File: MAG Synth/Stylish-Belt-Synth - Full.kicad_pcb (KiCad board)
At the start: 2 copper layers, 177.8 x 101.7 mm, 61 parts, among them J0 USB_B, J1 Audio-Jack-3_2Switches, J26 WRITE PATCH, J27 PARAM SELECT, J28 PATCH SELECT, J29 MODE, J30 STYLUS, SW1 Power, U1 stm32f103c8t6-module-china, U2 XPT8871

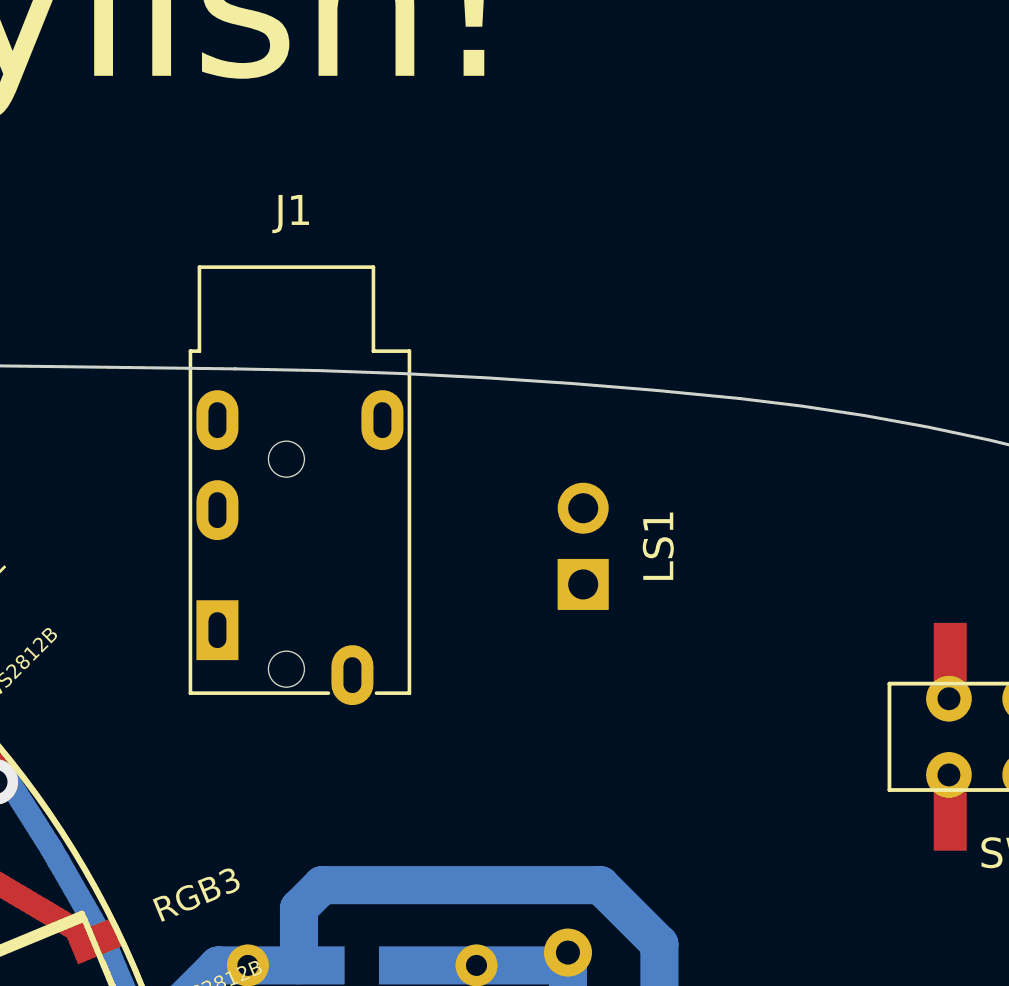
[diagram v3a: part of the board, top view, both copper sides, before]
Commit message: Updated footprints. Including STL for speaker holder.
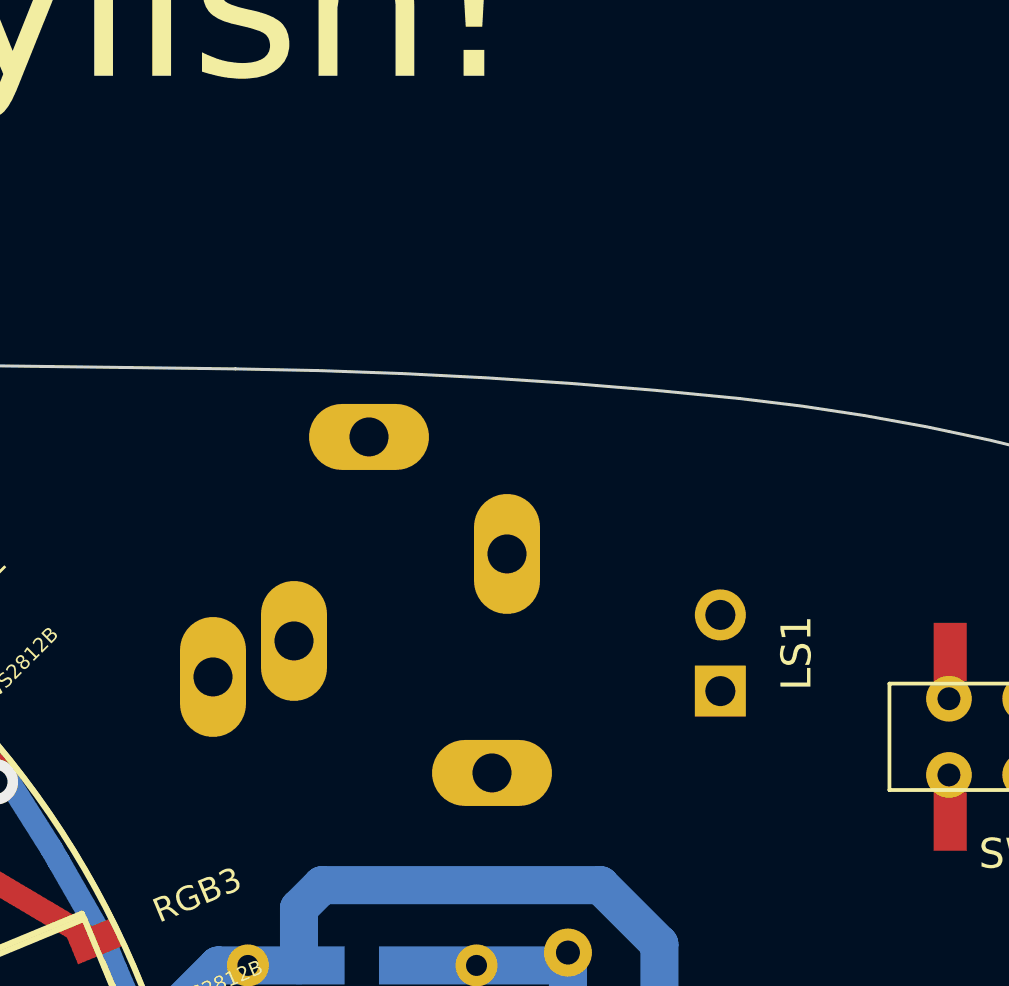
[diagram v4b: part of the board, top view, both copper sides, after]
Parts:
- J1: footprint Connectors:PJ320E_3.5mm_Jack -> Connectors:Stereo_Jack_3.5mm_Switch_Ledino_KB3SPRS; moved to B.Cu
- moved J1 9.98 mm to (188.5, 60.5), turned to 270 degrees
- moved LS1 5.79 mm to (195.6, 65.0)
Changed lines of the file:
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@@
     (add_net "Net-(U1-Pad38)")
   )
+  (module Connectors:Stereo_Jack_3.5mm_Switch_Ledino_KB3SPRS (layer B.Cu)
+    (at 188.468 60.452 270)
+    (descr https://www.reichelt.de/index.html?ACTION=7&LA=3&OPEN=0&INDEX=0&FILENAME=C160%252FKB3SPRS.pdf)
+    (tags "jack stereo TRS")
+    (fp_text reference J1 (at 2.54 13.97 270) (layer B.SilkS)
+      (effects (font (size 1 1) (thickness 0.15)) (justify mirror))
+    )
+    (fp_text value Audio-Jack-3_2Switches (at 2.54 -5.08 270) (layer B.Fab)
+      (effects (font (size 1 1) (thickness 0.15)) (justify mirror))
+    )
+    (fp_line (start -9.3 7.6) (end -9.3 1.6) (layer B.Fab) (width 0.1))
+    (fp_line (start -9.3 1.6) (end -5.7 1.6) (layer B.Fab) (width 0.1))
+    (fp_line (start -9.3 7.6) (end -5.7 7.6) (layer B.Fab) (width 0.1))
+    (fp_line (start -5.7 10.7) (end -5.7 -0.9) (layer B.Fab) (width 0.1))
+    (fp_line (start -5.7 -0.9) (end 8.6 -0.9) (layer B.Fab) (width 0.1))
+    (fp_line (start 8.6 -0.9) (end 8.6 10.7) (layer B.Fab) (width 0.1))
+    (fp_line (start 8.6 10.7) (end -5.7 10.7) (layer B.Fab) (width 0.1))
+    (fp_text user %R (at 2.54 13.97 270) (layer B.Fab)
+      (effects (font (size 1 1) (thickness 0.15)) (justify mirror))
+    )
+    (fp_line (start -9.8 -2) (end 9.1 -2) (layer B.CrtYd) (width 0.05))
+    (fp_line (start 9.1 11.4) (end -9.8 11.4) (layer B.CrtYd) (width 0.05))
+    (fp_line (start -5.8 10.8) (end 2.2 10.8) (layer B.SilkS) (width 0.15))
+    (fp_line (start 6 10.8) (end 8.7 10.8) (layer B.SilkS) (width 0.15))
+    (fp_line (start 8.7 10.8) (end 8.7 -1) (layer B.SilkS) (width 0.15))
+    (fp_line (start 8.7 -1) (end 8.6 -1) (layer B.SilkS) (width 0.15))
+    (fp_line (start 6 -1) (end 1.9 -1) (layer B.SilkS) (width 0.15))
+    (fp_line (start -1.9 -1) (end -5.8 -1) (layer B.SilkS) (width 0.15))
+    (fp_line (start -5.8 -1) (end -5.8 10.8) (layer B.SilkS) (width 0.15))
+    (fp_line (start -5.8 7.7) (end -9.4 7.7) (layer B.SilkS) (width 0.15))
+    (fp_line (start -9.4 7.7) (end -9.4 1.5) (layer B.SilkS) (width 0.15))
+    (fp_line (start -9.4 1.5) (end -5.8 1.5) (layer B.SilkS) (width 0.15))
+    (fp_line (start -9.8 11.4) (end -9.8 -2) (layer B.CrtYd) (width 0.05))
+    (fp_line (start 9.1 -2) (end 9.1 11.4) (layer B.CrtYd) (width 0.05))
+    (pad 1 thru_hole oval (at 0 0 270) (size 4 2.2) (drill 1.3) (layers *.Cu *.Mask)
+      (net 4 /XH-M125-amp-board/OUT+))
+    (pad 4 thru_hole oval (at 7.3 0.5 180) (size 4 2.2) (drill 1.3) (layers *.Cu *.Mask)
+      (net 22 "Net-(J1-Pad4)"))
+    (pad 5 thru_hole oval (at 2.9 7.1 270) (size 4 2.2) (drill 1.3) (layers *.Cu *.Mask)
+      (net 22 "Net-(J1-Pad4)"))
+    (pad 2 thru_hole oval (at 4.1 9.8 270) (size 4 2.2) (drill 1.3) (layers *.Cu *.Mask)
+      (net 4 /XH-M125-amp-board/OUT+))
+    (pad 3 thru_hole oval (at -3.9 4.6 270) (size 2.2 4) (drill 1.3) (layers *.Cu *.Mask)
+      (net 3 /XH-M125-amp-board/OUT-))
+    (model ${KISYS3DMOD}/Connectors.3dshapes/Stereo_Jack_3.5mm_Switch_Ledino_KB3SPRS.wrl
+      (at (xyz 0 0 0))
+      (scale (xyz 1 1 1))
+      (rotate (xyz 0 0 0))
+    )
+  )
   (module SVTmaker:MSS22D18+THT (layer F.Cu)
     (at 205.74 66.548 180)
@@
   )
   (module Pin_Headers:Pin_Header_Straight_1x02_Pitch2.54mm (layer B.Cu)
-    (at 191.008 61.468)
+    (at 195.58 65.024)
     (descr "Through hole straight pin header, 1x02, 2.54mm pitch, single row")
     (tags "Through hole pin header THT 1x02 2.54mm single row")
@@
     )
   )
-  (module Connectors:PJ320E_3.5mm_Jack (layer F.Cu)
-    (at 178.816 62.992)
-    (descr "Headphones with microphone connector, 3.5mm, 4 pins.")
-    (tags "3.5mm jack mic microphone phones headphones 4pins audio plug")
-    (fp_text reference J1 (at 2.54 -13.97) (layer F.SilkS)
-      (effects (font (size 1 1) (thickness 0.15)))
-    )
-    (fp_text value Audio-Jack-3_2Switches (at 2.54 5.08) (layer F.Fab)
-      (effects (font (size 1 1) (thickness 0.15)))
-    )
-    (fp_line (start -1.3 -12.5) (end 6.8 -12.5) (layer F.CrtYd) (width 0.05))
-    (fp_line (start -0.6 -9.3) (end -0.6 -12.1) (layer F.SilkS) (width 0.12))
-    (fp_line (start 5.2 -9.3) (end 5.2 -12.1) (layer F.SilkS) (width 0.12))
-    (fp_line (start 6.4 -9.3) (end 6.4 2.1) (layer F.SilkS) (width 0.12))
-    (fp_line (start 5.2 -12.1) (end -0.6 -12.1) (layer F.SilkS) (width 0.12))
-    (fp_line (start -0.9 -9.3) (end -0.6 -9.3) (layer F.SilkS) (width 0.12))
-    (fp_line (start 5.2 -9.3) (end 6.4 -9.3) (layer F.SilkS) (width 0.12))
-    (fp_line (start 6.8 -12.5) (end 6.8 3) (layer F.CrtYd) (width 0.05))
-    (fp_line (start -1.3 -12.5) (end -1.3 3) (layer F.CrtYd) (width 0.05))
-    (fp_line (start -1.3 3) (end 6.8 3) (layer F.CrtYd) (width 0.05))
-    (fp_line (start 6.4 2.1) (end 5.3 2.1) (layer F.SilkS) (width 0.12))
-    (fp_line (start -0.9 2.1) (end 3.7 2.1) (layer F.SilkS) (width 0.12))
-    (fp_line (start -0.9 -9.3) (end -0.9 2.1) (layer F.SilkS) (width 0.12))
-    (fp_line (start 6.3 2) (end 5.3 2) (layer F.Fab) (width 0.1))
-    (fp_line (start 6.3 -9.2) (end 6.3 2) (layer F.Fab) (width 0.1))
-    (fp_line (start 5.1 -9.2) (end 6.3 -9.2) (layer F.Fab) (width 0.1))
-    (fp_line (start 5.1 -12) (end 5.1 -9.2) (layer F.Fab) (width 0.1))
-    (fp_line (start -0.5 -12) (end 5.1 -12) (layer F.Fab) (width 0.1))
-    (fp_line (start -0.5 -9.2) (end -0.5 -12) (layer F.Fab) (width 0.1))
-    (fp_line (start -0.8 -9.2) (end -0.5 -9.2) (layer F.Fab) (width 0.1))
-    (fp_line (start -0.8 2) (end -0.8 -9.2) (layer F.Fab) (width 0.1))
-    (fp_line (start 3.7 2) (end -0.8 2) (layer F.Fab) (width 0.1))
-    (fp_text user %R (at 2.54 -13.97) (layer F.Fab)
-      (effects (font (size 1 1) (thickness 0.15)))
-    )
-    (pad "" np_thru_hole circle (at 2.3 1.3 270) (size 1.2 1.2) (drill 1.2) (layers *.Cu *.Mask))
-    (pad "" np_thru_hole circle (at 2.3 -5.7 270) (size 1.2 1.2) (drill 1.2) (layers *.Cu *.Mask))
-    (pad 3 thru_hole oval (at 0 -7 270) (size 2 1.4) (drill oval 1.2 0.6) (layers *.Cu *.Mask)
-      (net 3 /XH-M125-amp-board/OUT-))
-    (pad 2 thru_hole oval (at 0 -4 270) (size 2 1.4) (drill oval 1.2 0.6) (layers *.Cu *.Mask)
-      (net 4 /XH-M125-amp-board/OUT+))
-    (pad 1 thru_hole rect (at 0 0 270) (size 2 1.4) (drill oval 1.2 0.6) (layers *.Cu *.Mask)
-      (net 4 /XH-M125-amp-board/OUT+))
-    (pad 4 thru_hole oval (at 4.5 1.5 270) (size 2 1.4) (drill oval 1.2 0.6) (layers *.Cu *.Mask)
-      (net 22 "Net-(J1-Pad4)"))
-    (pad 5 thru_hole oval (at 5.5 -7 270) (size 2 1.4) (drill oval 1.2 0.6) (layers *.Cu *.Mask)
-      (net 22 "Net-(J1-Pad4)"))
-  )
   (gr_text Stylish! (at 189.6364 67.1957) (layer F.Mask)

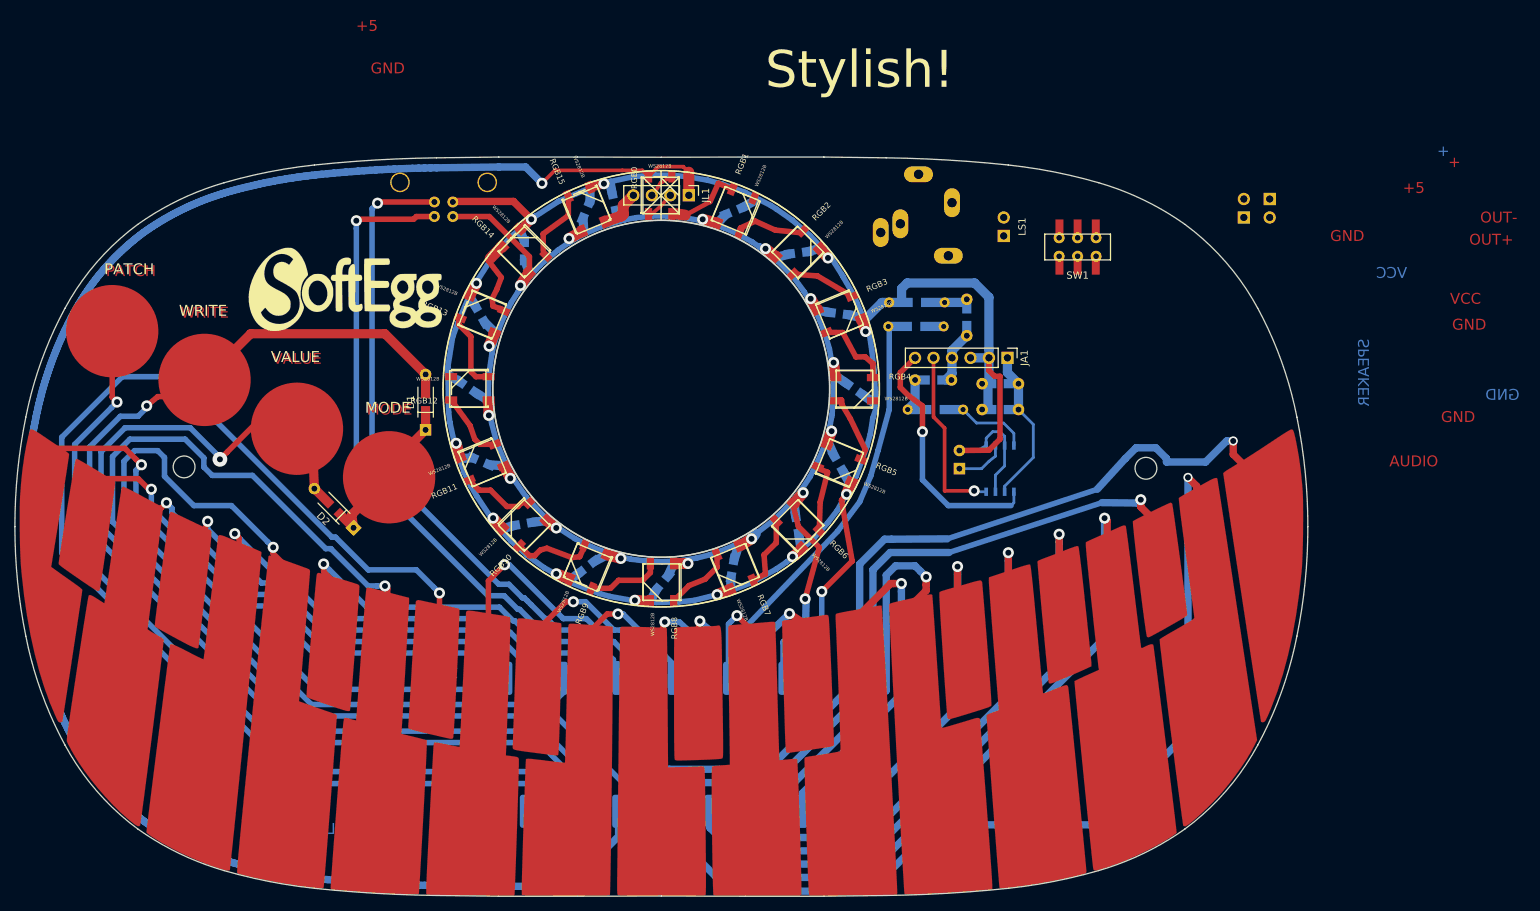
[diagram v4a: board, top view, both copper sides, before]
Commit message: V0.2 PCB completed! Schematic, PCB, and Gerbers updated.
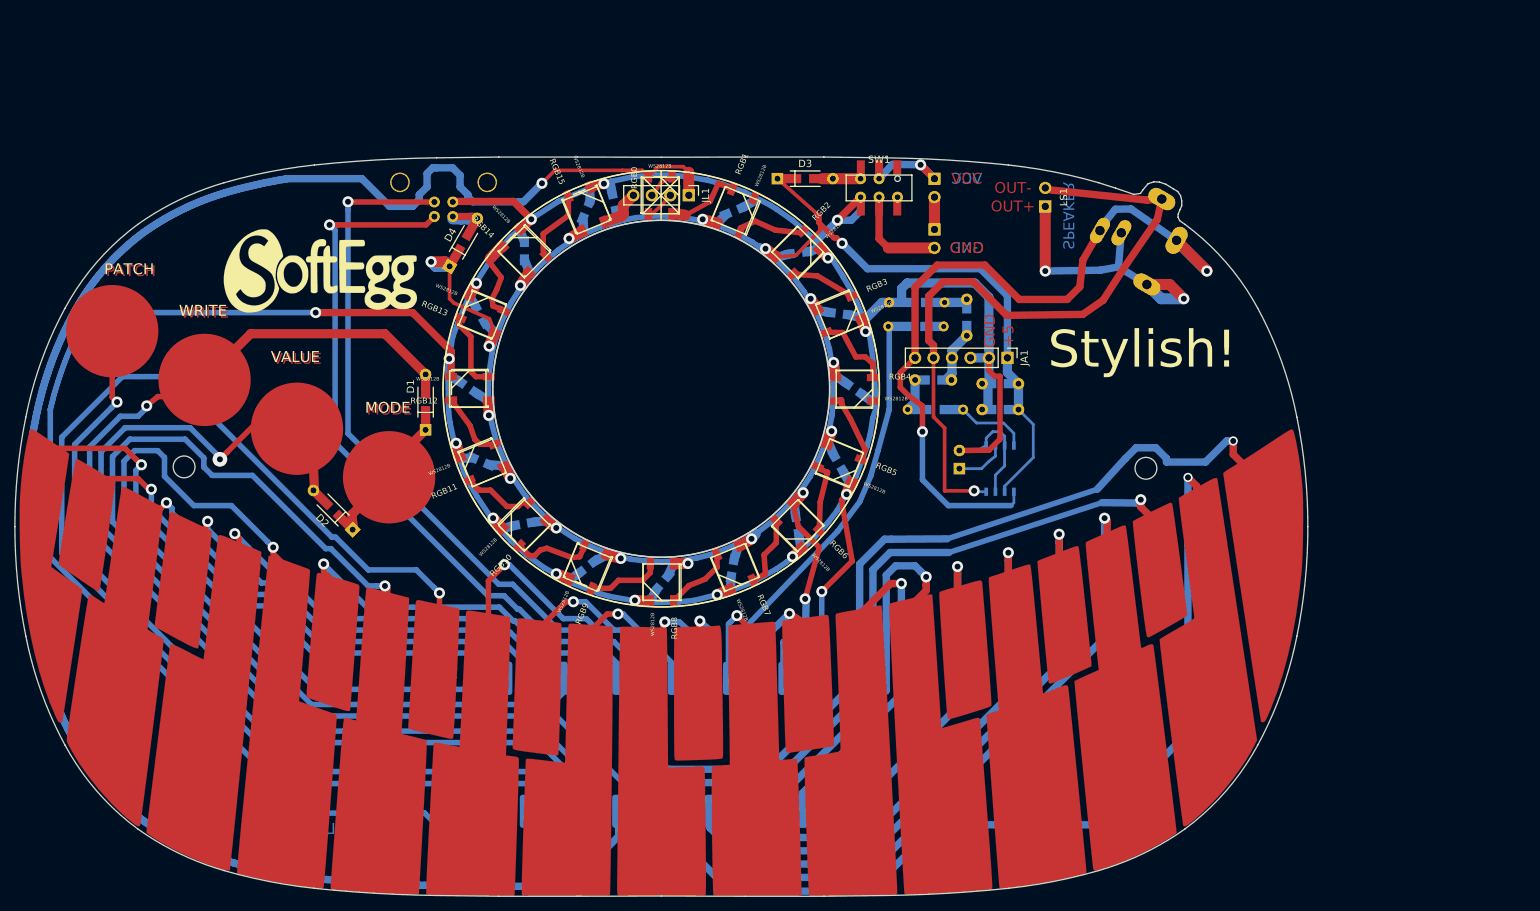
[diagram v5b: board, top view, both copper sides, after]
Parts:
- added D3: 1N5822, SoftEggKiCAD:D_DO-35_SOD27_P7.62mm_Horizontal+SMD, F.Cu at (164.5, 57.1)
- added D4: 1N5822, SoftEggKiCAD:D_DO-35_SOD27_P7.62mm_Horizontal+SMD, F.Cu at (119.4, 69.2)
- C1, CA2, CA3: value 1uF -> 1μF
- CA1: value 470uF -> 470μF
- CA4: value 0.39uF -> 0.39μF
- R1: value 10k -> 10kΩ
- R3: value R -> 100Ω
- SW1: footprint SVTmaker:MSS22D18+THT -> SoftEggKiCAD:MSS22D18+THT
- moved BT2 46.3 mm to (186.1, 64.1)
- moved BT1 42.9 mm to (186.1, 57.1), turned to 180 degrees
- moved J1 31.3 mm to (219.3, 65.6), turned to 240 degrees
- moved SW1 28.5 mm to (178.4, 58.4), turned to 0 degrees
- moved LS1 7.01 mm to (201.3, 61.0)
- moved G*** 4.27 mm to (101.6, 69.8)
- moved D2 0.28 mm to (106.0, 105.4)
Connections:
- BT1 pad 2: GND -> Net-(BT1-Pad2)
- BT2 pad 1: GND -> Net-(BT1-Pad2)
- BT2 pad 2: Net-(BT1-Pad1) -> Net-(BT2-Pad2)
- J0 pad 1: /+5V -> Net-(D4-Pad2)
- SW1 pad P1: (no net) -> Net-(BT1-Pad1)
- SW1 pad P2: (no net) -> Net-(BT2-Pad2)
- SW1 pad T1A: (no net) -> Net-(D3-Pad2)
- SW1 pad T1B: (no net) -> Net-(SW1-PadT1B)
- SW1 pad T2A: (no net) -> GND
- SW1 pad T2B: (no net) -> Net-(SW1-PadT2B)
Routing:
- net GND: track 360.9 -> 543.1 mm, vias 13 -> 16
- net /XH-M125-amp-board/OUT+: track 34.8 -> 104.7 mm, vias 1 -> 2
- net /XH-M125-amp-board/OUT-: track 24.7 -> 92.5 mm
- net /+5V: track 275.0 -> 336.9 mm, vias 16 -> 18
- net Net-(J1-Pad4): track 0.00 -> 49.0 mm, vias 0 -> 2
- net Net-(BT1-Pad1): track 0.00 -> 14.7 mm, vias 0 -> 1
- net Net-(BT2-Pad2): track 0.00 -> 13.9 mm
- net /LED_DIN: track 247.7 -> 256.1 mm
- net Net-(D4-Pad2): track 0.00 -> 6.87 mm
- net Net-(D3-Pad2): track 0.00 -> 5.33 mm
- net Net-(J0-Pad2): track 92.7 -> 97.6 mm
- net Net-(BT1-Pad2): track 0.00 -> 4.45 mm
- net Net-(J0-Pad3): track 93.4 -> 97.5 mm
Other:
- outline, holes or cut-outs redrawn
- board text removed: "+"
- board text removed: "AUDIO"

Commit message: PCB tweaked a little. Zig zag cut line generated on User 1 layer. Souce code: state machine in progress.
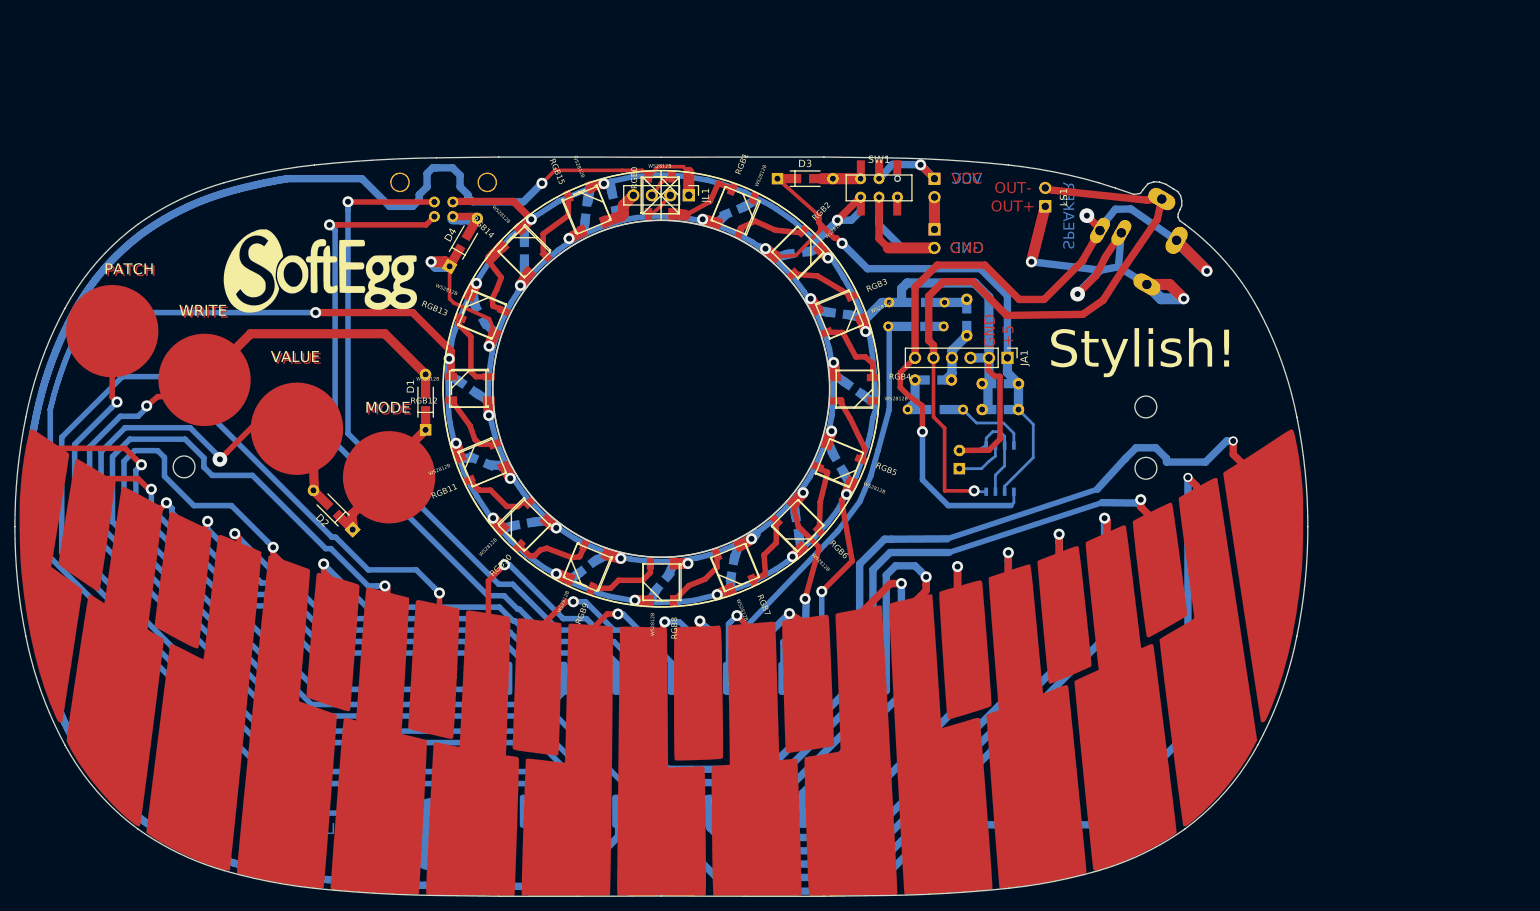
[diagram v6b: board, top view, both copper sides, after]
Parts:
- moved J30 5.92 mm to (117.5, 147.3)
- turned CL15 to 84 degrees
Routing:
- net Net-(J1-Pad4): track 49.0 -> 63.9 mm, vias 2 -> 3
- net Net-(BT2-Pad2): track 13.9 -> 26.6 mm
- net GND: track 543.1 -> 536.6 mm
- net /XH-M125-amp-board/OUT+: track 104.7 -> 108.6 mm, vias 2 -> 3
- net Net-(D3-Pad2): track 5.33 -> 9.14 mm
- net /+5V: track 336.9 -> 337.9 mm
